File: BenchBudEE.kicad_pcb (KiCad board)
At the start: 4 copper layers, 165.1 x 63.5 mm, 11 parts, among them K1 RELAY, Q1 2N3904, U1 OPTO_TRANSISTOR

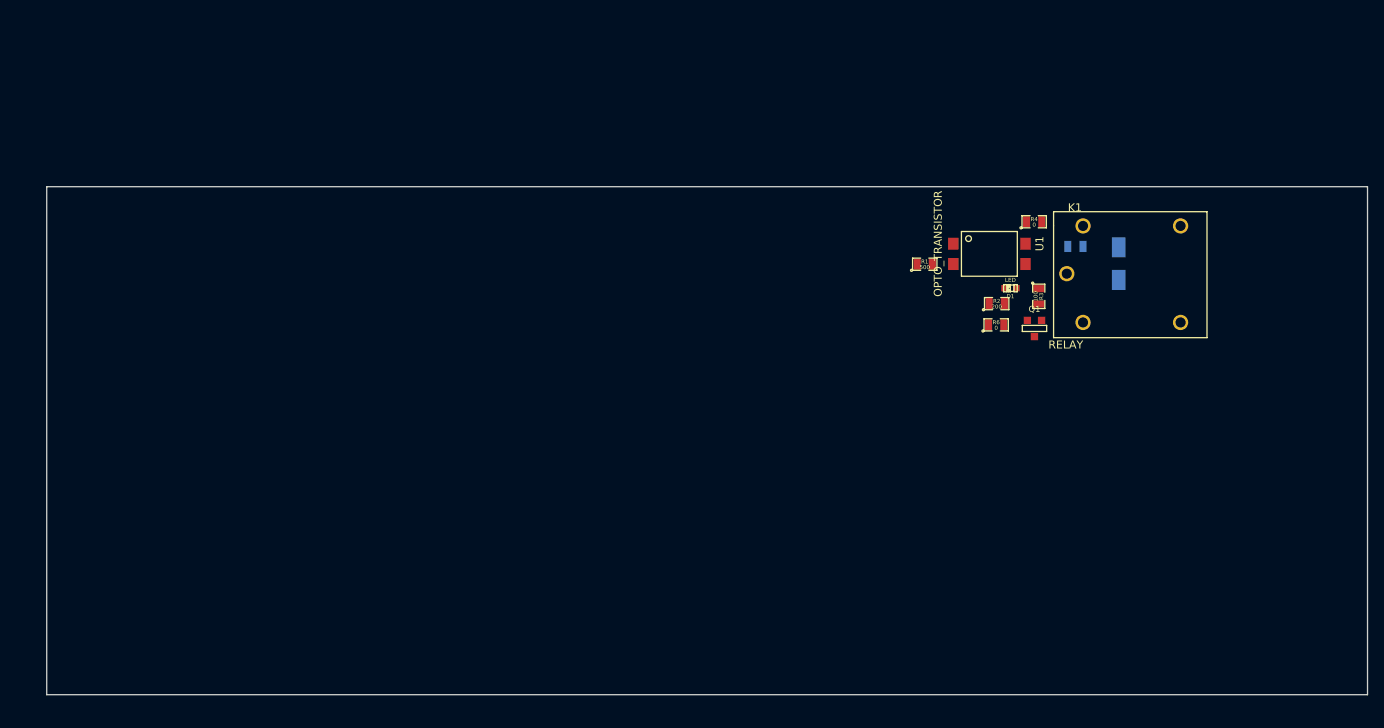
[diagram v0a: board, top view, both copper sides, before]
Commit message: THERMOCOUPLE 02-22-2014
Associated and placed PCB footprints of thermocouple modules in layout
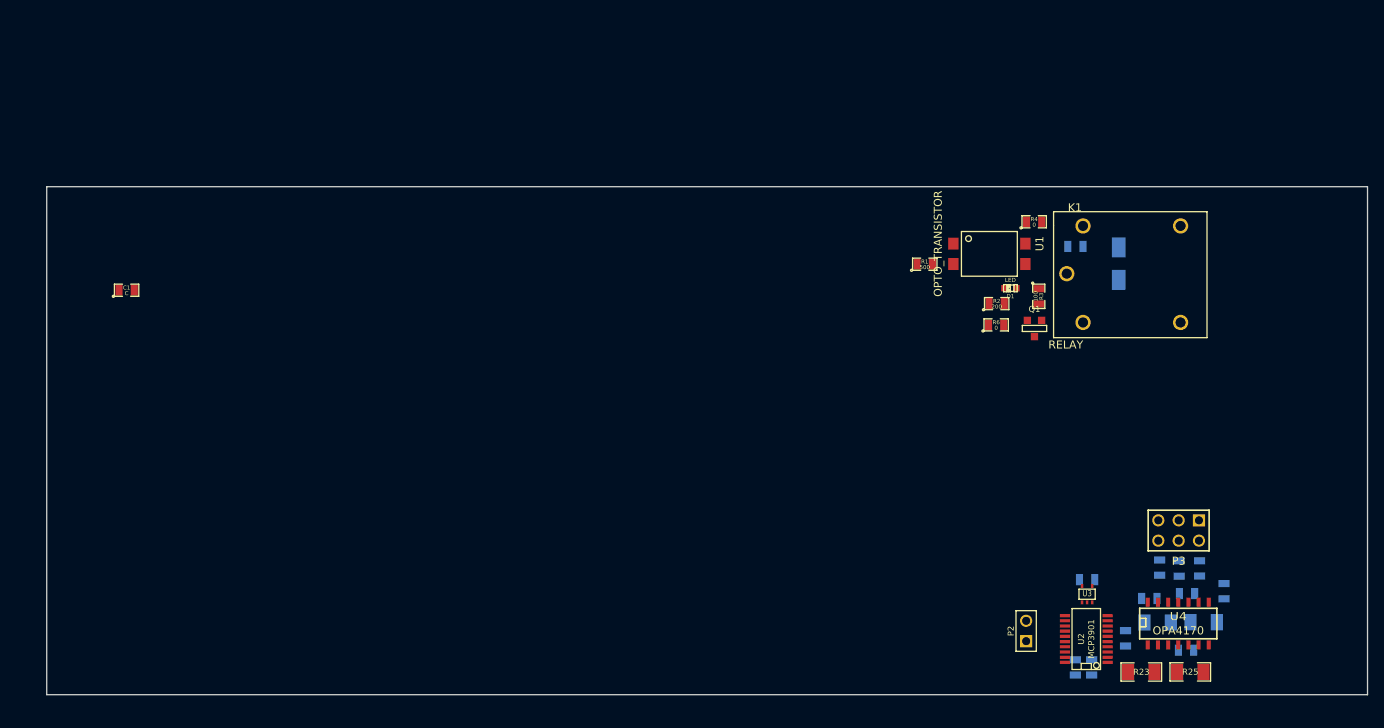
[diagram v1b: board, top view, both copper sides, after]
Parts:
- added C1: C, SM0805, F.Cu at (77.3, 134.1)
- added C10: C, SM0805, B.Cu at (209.7, 179.1)
- added C11: C, SM0805, B.Cu at (209.8, 172.0)
- added C6: C, SM0805, B.Cu at (197.9, 181.2)
- added C7: C, SM0805, B.Cu at (195.9, 181.2)
- added C8: C, SM0805, B.Cu at (202.1, 177.6)
- added C9: C, SM0805, B.Cu at (197.3, 170.2)
- added P2: CONN_2, PIN_ARRAY_2X1, F.Cu at (189.7, 176.7)
- added P3: CONN_3X2, pin_array_3x2, F.Cu at (208.8, 164.1)
- added R23: R, SM1206, F.Cu at (204.1, 181.8)
- added R24: R, SM1206, B.Cu at (211.9, 175.6)
- added R25: R, SM1206, F.Cu at (210.2, 181.8)
- added R26: R, SM1206, B.Cu at (206.2, 175.6)
- added R27: R, SM0805, B.Cu at (214.5, 171.7)
- added R28: R, SM0805, B.Cu at (206.4, 168.7)
- added R29: R, SM0805, B.Cu at (205.1, 172.6)
- added R44: R, SM0805, B.Cu at (208.8, 168.8)
- added R45: R, SM0805, B.Cu at (211.4, 168.8)
- added U2: MCP3901, SSOP20, F.Cu at (197.2, 177.7)
- added U3: LMT84, SOT353, F.Cu at (197.3, 172.1)
- added U4: OPA4170, SO14E, F.Cu at (208.7, 175.6)

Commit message: Terminal Blocks and ATX Connector
Created footprints for 12pin, 3pin terminal blocks and 24pin ATX Header.
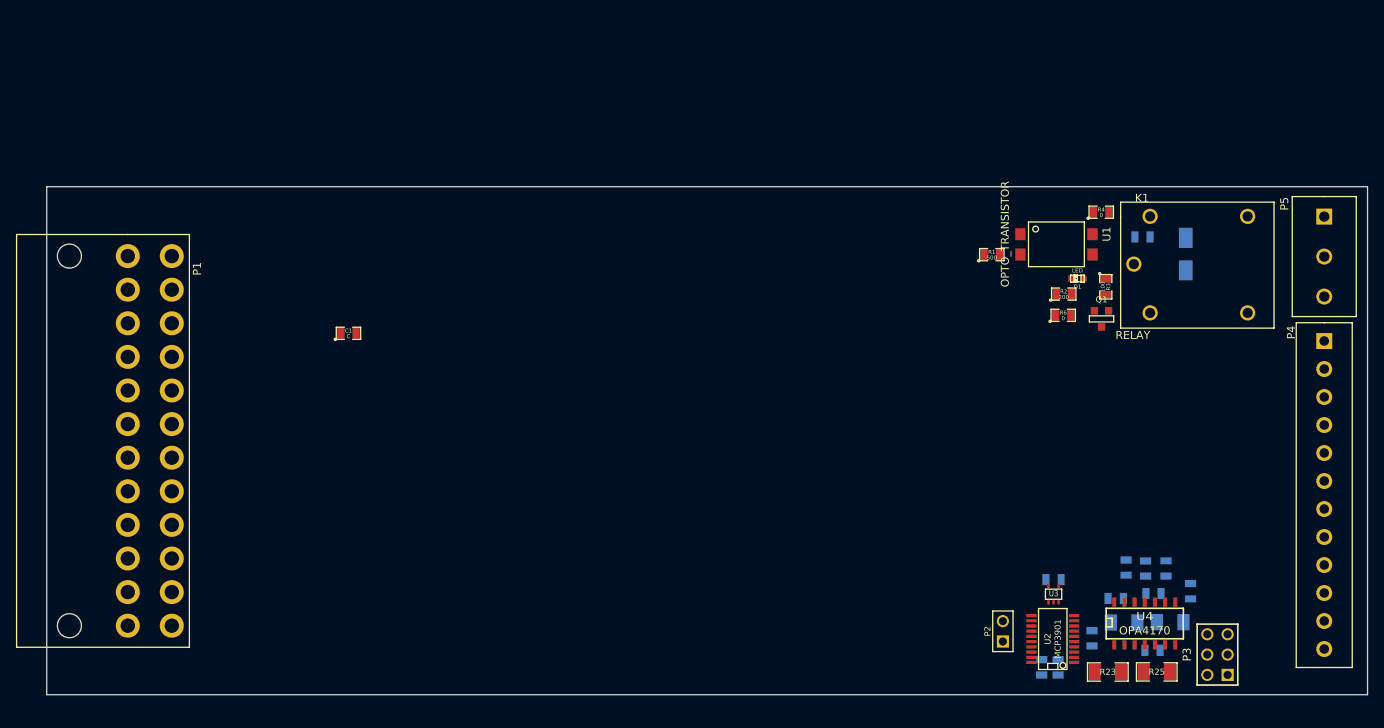
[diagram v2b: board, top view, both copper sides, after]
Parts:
- added P1: 24 Pin MiniFit JR, ATX_Header, F.Cu at (77.4, 129.8)
- added P4: 12 Pin Terminal Block, 12pin_TB, F.Cu at (227.0, 140.4)
- added P5: CONN_3, 3pin_TB, F.Cu at (227.0, 124.9)
- moved C1 28.3 mm to (105.0, 139.4)
- moved P3 16.2 mm to (213.6, 179.6), turned to 90 degrees
- moved D2 8.47 mm to (209.7, 131.6)
- moved Q1 8.47 mm to (199.1, 137.6)
- moved R3 8.47 mm to (199.7, 133.6)
- moved R4 8.47 mm to (199.1, 124.3)
- moved R5 8.47 mm to (204.3, 127.4)
- moved U1 8.47 mm to (189.0, 127.1)
- moved D1 8.47 mm to (196.1, 132.6)
- moved K1 8.47 mm to (203.2, 130.8)
- moved R2 8.47 mm to (194.4, 134.5)
- moved R1 8.47 mm to (185.4, 129.6)
- moved R6 8.47 mm to (194.3, 137.2)
- moved C10 4.19 mm to (205.5, 179.1)
- moved C11 4.19 mm to (205.6, 172.0)
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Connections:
- K1 pad 1: (no net) -> /Relay/RELAY_COM
- K1 pad 3: (no net) -> /Relay/RELAY_NO
- K1 pad 4: (no net) -> /Relay/RELAY_NC
- U4 pad 10: (no net) -> /Terminal_Block/TC_IN_+
- U4 pad 12: (no net) -> /Terminal_Block/TC_IN_-

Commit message: Fan Controller Module
1) Created and associated the footprints of fan controller module
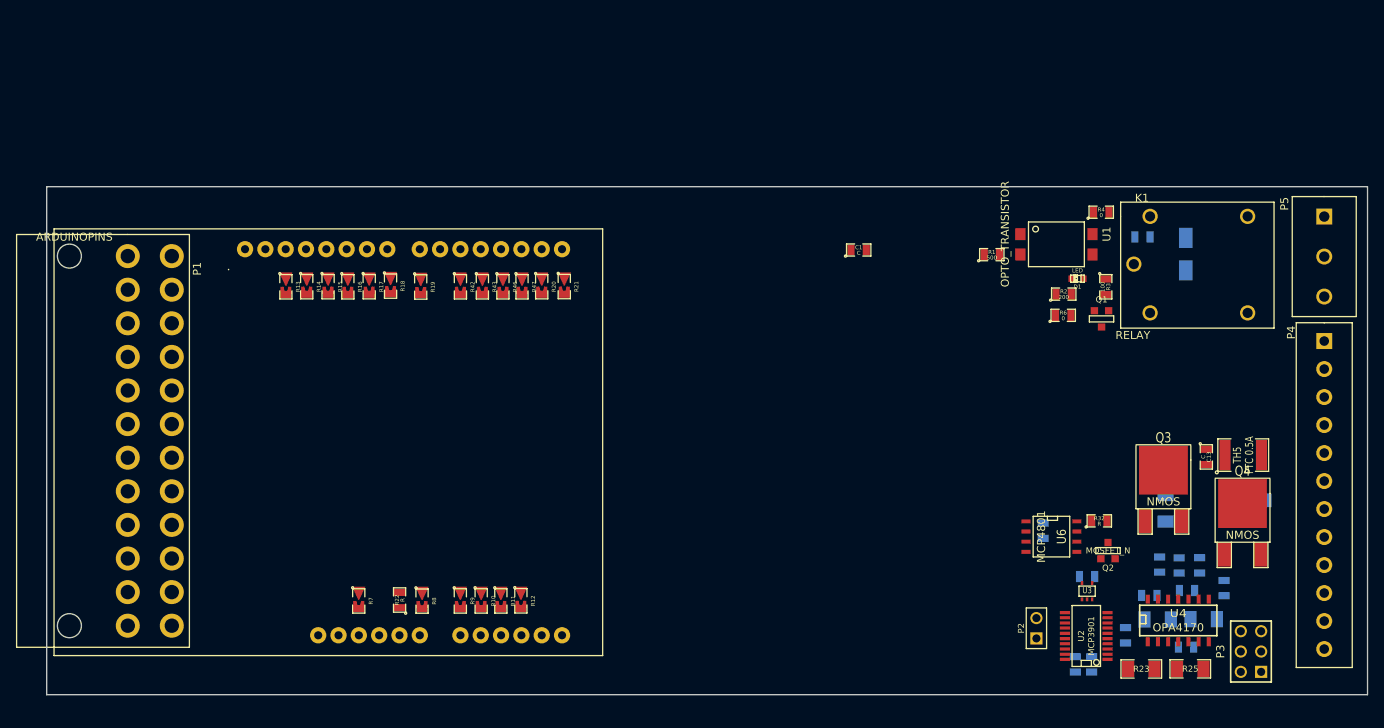
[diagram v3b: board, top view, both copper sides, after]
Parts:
- added ARD1: ARDUINOPINS, ARDUINO, F.Cu at (106.3, 177.2)
- added C12: C, SM0805, B.Cu at (191.8, 164.1)
- added C13: C, SM0805, F.Cu at (212.2, 154.9)
- added D5: Schottky Diode, SMA, B.Cu at (215.1, 160.3)
- added Q2: MOSFET_N, SOT23GDS, F.Cu at (199.9, 166.6)
- added Q3: NMOS, DPAK2, F.Cu at (206.9, 162.9)
- added Q4: NMOS, DPAK2, F.Cu at (216.8, 167.1)
- added R10: R, SM0805-bridge, F.Cu at (121.6, 172.9)
- added R11: R, SM0805-bridge, F.Cu at (124.1, 172.9)
- added R12: R, SM0805-bridge, F.Cu at (126.6, 172.9)
- added R13: R, SM0805-bridge, F.Cu at (97.2, 133.6)
- added R14: R, SM0805-bridge, F.Cu at (99.8, 133.6)
- added R15: R, SM0805-bridge, F.Cu at (102.5, 133.6)
- added R16: R, SM0805-bridge, F.Cu at (104.9, 133.6)
- added R17: R, SM0805-bridge, F.Cu at (107.6, 133.6)
- added R18: R, SM0805-bridge, F.Cu at (110.3, 133.5)
- added R19: R, SM0805-bridge, F.Cu at (114.0, 133.7)
- added R20: R, SM0805-bridge, F.Cu at (129.2, 133.6)
- added R21: R, SM0805-bridge, F.Cu at (132.0, 133.6)
- added R22: R, SM0805, F.Cu at (111.4, 172.8)
- added R32: R, SM0805, F.Cu at (198.9, 162.9)
- added R33: R, SM1206, B.Cu at (207.1, 161.3)
- added R42: R, SM0805-bridge, F.Cu at (119.0, 133.6)
- added R43: R, SM0805-bridge, F.Cu at (121.7, 133.6)
- added R46: R, SM0805-bridge, F.Cu at (124.3, 133.6)
- added R47: R, SM0805-bridge, F.Cu at (126.7, 133.6)
- added R7: R, SM0805-bridge, F.Cu at (106.3, 172.9)
- added R8: R, SM0805-bridge, F.Cu at (114.2, 172.9)
- added R9: R, SM0805-bridge, F.Cu at (119.0, 172.9)
- added TH5: PTC 0.5A, SM1812, F.Cu at (216.8, 154.7)
- added U6: MCP4801, SO8N, F.Cu at (192.9, 164.9)
- moved C1 64.6 mm to (168.8, 129.0)
- moved C10 4.21 mm to (209.7, 178.7)
- moved C11 4.21 mm to (209.8, 171.6)
- moved C6 4.21 mm to (197.9, 180.8)
- moved C7 4.21 mm to (195.9, 180.8)
- moved C9 4.21 mm to (197.3, 169.8)
- moved P3 4.21 mm to (217.8, 179.2)
- moved R23 4.21 mm to (204.1, 181.4)
- moved R25 4.21 mm to (210.2, 181.4)
- moved R26 4.21 mm to (206.2, 175.2)
- moved R27 4.21 mm to (214.5, 171.3)
- moved R28 4.21 mm to (206.4, 168.4)
- moved R29 4.21 mm to (205.1, 172.2)
- moved R44 4.21 mm to (208.8, 168.5)
- moved R45 4.21 mm to (211.4, 168.5)
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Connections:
- U2 pad 17: /Arduino/ADC_CS_N -> /Arduino/~ADC_CS

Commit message: Power Filter Module
Created and associated footprints for PCB layout
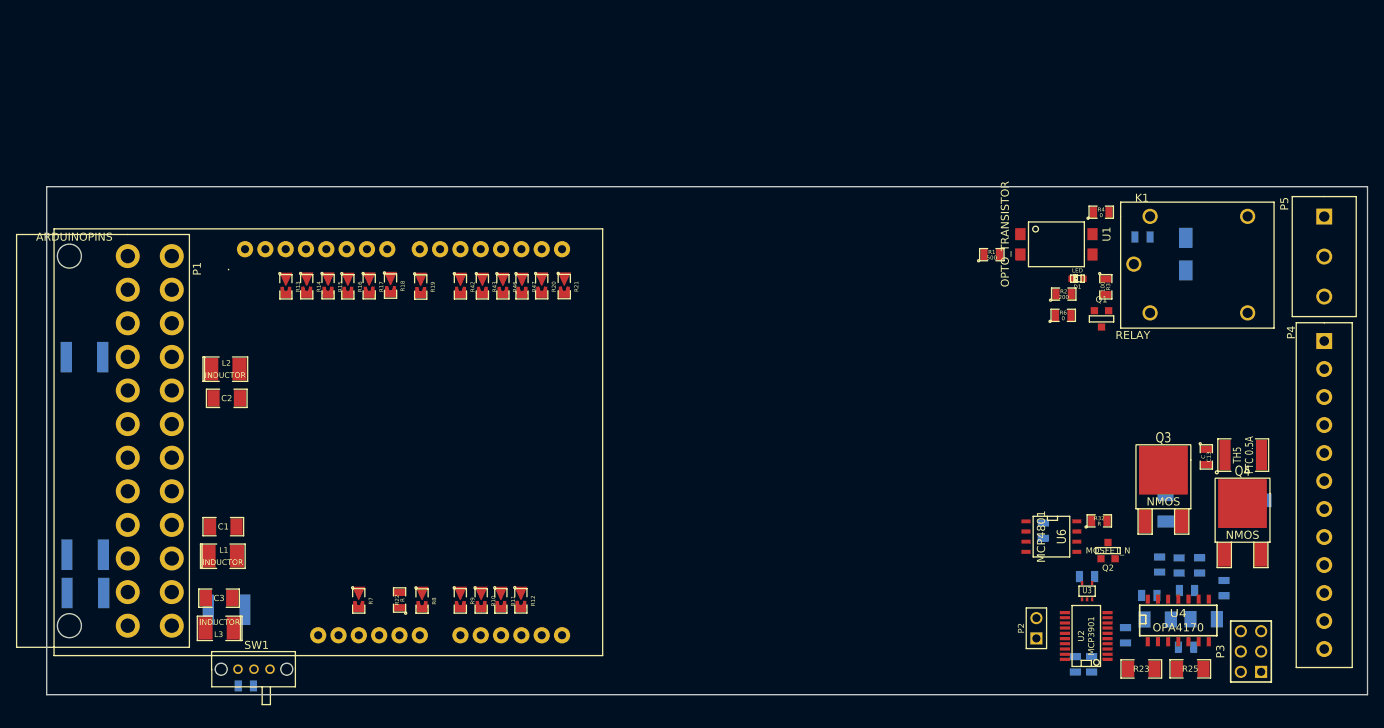
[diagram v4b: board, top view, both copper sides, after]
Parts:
- added C2: C, SM1206, F.Cu at (89.8, 147.6)
- added C3: C, SM1206, F.Cu at (88.8, 172.6)
- added L1: INDUCTOR, SM1210L, F.Cu at (89.3, 167.3)
- added L2: INDUCTOR, SM1210L, F.Cu at (89.6, 143.9)
- added L3: INDUCTOR, SM1210L, F.Cu at (88.9, 176.3)
- added R30: R, SM0805, B.Cu at (92.2, 183.5)
- added SW1: SWITCH, SPDT_SW, F.Cu at (93.2, 181.4)
- added TH1: THERMISTOR, SM1812, B.Cu at (72.1, 171.9)
- added TH2: THERMISTOR, SM1812, B.Cu at (72.1, 167.1)
- added TH3: THERMISTOR, SM1812, B.Cu at (72.0, 142.4)
- added TH4: THERMISTOR, SM1812, B.Cu at (89.8, 174.0)
- C1: footprint SM0805 -> SM1206
- moved C1 86.6 mm to (89.4, 163.6), turned to 180 degrees

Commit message: Completed placement and association of all footprints
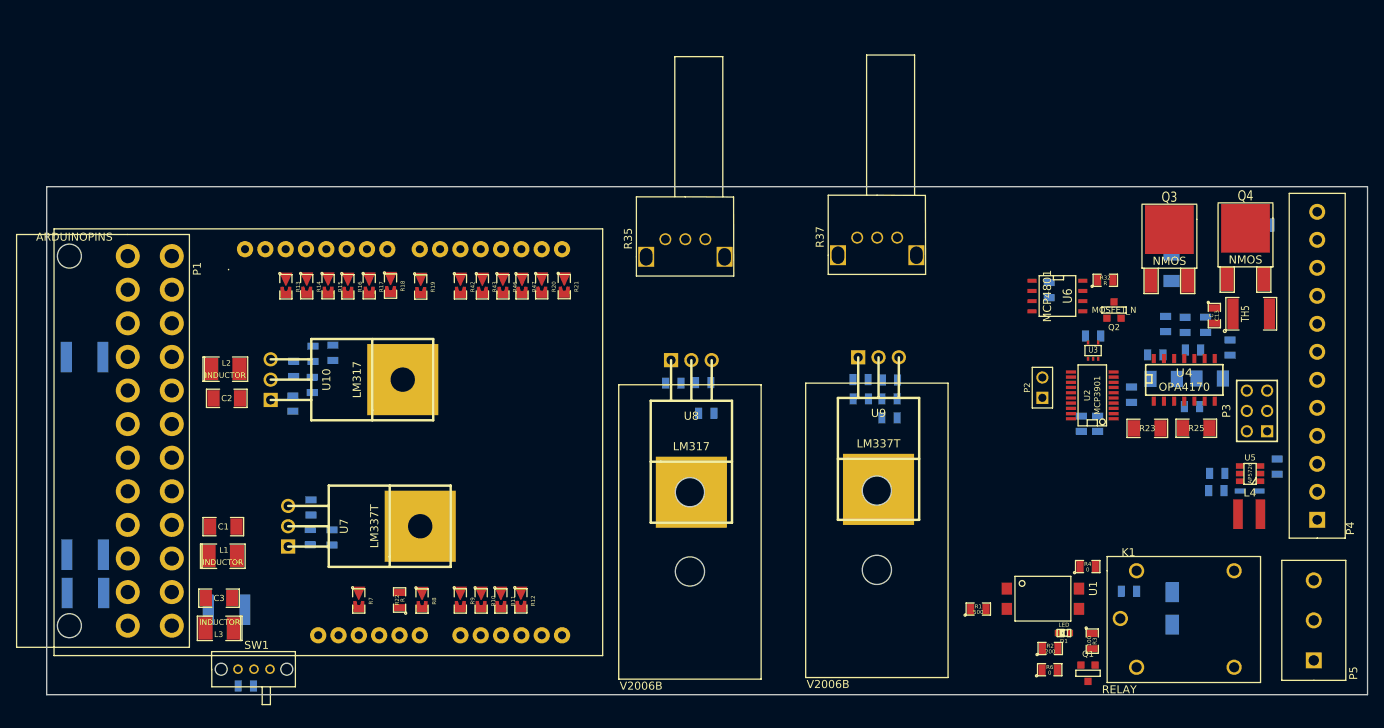
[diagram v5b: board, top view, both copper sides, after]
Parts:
- added C14: C, SM0805, B.Cu at (169.0, 145.2)
- added C15: C, SM0805, B.Cu at (98.0, 148.2)
- added C16: C, SM0805, B.Cu at (100.3, 161.2)
- added C17: C, SM0805, B.Cu at (100.5, 145.9)
- added C18: C, SM0805, B.Cu at (145.6, 145.7)
- added C19: C, SM0805, B.Cu at (172.6, 150.0)
- added C4: 1u, SM0805, B.Cu at (213.5, 159.1)
- added C5: 1u, SM0805, B.Cu at (213.6, 157.0)
- added D4: B0540WS-7, SOD323, B.Cu at (218.8, 159.2)
- added L4: 22uH, NR4012, F.Cu at (216.2, 162.1)
- added R31: 15, SM0805, B.Cu at (221.1, 156.1)
- added R34: R, SM0805, B.Cu at (149.3, 145.6)
- added R35: RVAR, POT_EVUE3K, F.Cu at (147.1, 127.7)
- added R36: R, SM0805, B.Cu at (172.7, 145.3)
- added R37: RVAR, POT_EVUE3K, F.Cu at (171.1, 127.5)
- added R38: R, SM0805, B.Cu at (149.7, 149.4)
- added R39: R, SM0805, B.Cu at (103.0, 141.9)
- added R40: R, SM0805, B.Cu at (172.6, 147.6)
- added R41: R, SM0805, B.Cu at (169.0, 147.6)
- added R48: R, SM0805, B.Cu at (102.9, 165.0)
- added R49: R, SM0805, B.Cu at (100.2, 164.9)
- added R50: R, SM0805, B.Cu at (98.1, 143.9)
- added R51: R, SM0805, B.Cu at (100.6, 142.0)
- added U10: LM317, TO220, F.Cu at (95.3, 145.2)
- added U5: AP5726, SOT23_6, F.Cu at (217.7, 157.0)
- added U7: LM337T, TO220, F.Cu at (97.5, 163.6)
- added U8: LM317, TO220, F.Cu at (147.9, 142.8)
- added U9: LM337T, TO220, F.Cu at (171.3, 142.4)
- added V2006B: VAL**, V2006B, F.Cu at (162.2, 182.5)
- added V2006B: VAL**, V2006B, F.Cu at (138.8, 182.7)
- moved P5 55.5 mm to (225.7, 180.3), turned to 90 degrees
- moved Q1 44.3 mm to (197.4, 181.9)
- moved R1 44.3 mm to (183.7, 173.9)
- moved R5 44.3 mm to (202.6, 171.7)
- moved R4 44.3 mm to (197.4, 168.6)
- moved U1 44.3 mm to (187.3, 171.3)
- moved D1 44.3 mm to (194.4, 176.9)
- moved D2 44.3 mm to (208.0, 175.9)
- moved K1 44.3 mm to (201.5, 175.1)
- moved R2 44.3 mm to (192.7, 178.8)
- moved R3 44.3 mm to (198.0, 177.9)
- moved R6 44.3 mm to (192.7, 181.5)
- moved D5 34.4 mm to (215.4, 125.9)
- moved Q4 34.4 mm to (217.1, 132.7)
- moved C10 30.1 mm to (210.4, 148.6)
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
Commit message: Layout v1.0
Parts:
- removed V2006B (x2): VAL**, V2006B
- added 3mm_drill: VAL**, 3mm_drill, F.Cu at (80.1, 124.1)
- added 3mm_drill: VAL**, 3mm_drill, F.Cu at (80.3, 181.6)
- added 3mm_drill: VAL**, 3mm_drill, F.Cu at (218.1, 126.2)
- added JP1: JUMPER, PIN_ARRAY_2X1, F.Cu at (212.5, 162.3)
- U10, U8: value LM317 -> LM317K; footprint TO220 -> TO220_VERT
- U7, U9: footprint TO220 -> TO220_VERT
- moved R49 85.2 mm to (179.9, 134.7), turned to 0 degrees
- moved R48 83.8 mm to (180.0, 132.0), turned to 180 degrees
- moved U10 83.2 mm to (178.4, 148.9), turned to 90 degrees
- moved C16 80.4 mm to (176.2, 134.7), turned to 0 degrees
- moved C15 71.0 mm to (167.9, 135.8), turned to 0 degrees
- moved U7 68.6 mm to (164.6, 149.4), turned to 90 degrees
- moved C17 66.3 mm to (165.6, 133.4), turned to 0 degrees
- moved R50 65.9 mm to (163.6, 135.7), turned to 180 degrees
- moved R51 61.8 mm to (161.7, 133.3), turned to 180 degrees
- moved R39 59.6 mm to (161.6, 130.8), turned to 180 degrees
- moved C6 53.0 mm to (148.0, 166.5)
- moved C7 53.0 mm to (146.0, 166.5)
- moved U2 53.0 mm to (147.3, 162.9)
- moved P2 53.0 mm to (141.1, 162.0)
- moved C8 53.0 mm to (152.2, 162.8)
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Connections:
- C13 pad 2: AGND -> GND
- K1 pad 3: /Relay/RELAY_NO -> /Relay/RELAY_NC
- K1 pad 4: /Relay/RELAY_NC -> /Relay/RELAY_NO
- Q3 pad 3: AGND -> GND
- R33 pad 2: AGND -> GND
- R34 pad 2: N-00000118 (its old number) -> N-00000120
- R35 pad 1: N-00000118 (its old number) -> N-00000120
- R50 pad 2: N-00000122 -> N-00000121
- R51 pad 1: N-00000122 -> N-00000121
- TH1 pad 2: (no net) -> +3.3V
- U10 pad 1: +12V -> N-00000120
- U10 pad 2: N-00000122 -> +12V
- U10 pad 3: FE_V+ -> /Power_Adjustment_Monitor/V+_ADJ
- U4 pad 11: -12V -> FE_V-
- U4 pad 4: +12V -> FE_V+
- U8 pad 1: +12V -> N-00000121
- U8 pad 2: N-00000118 (its old number) -> +12V
- U8 pad 3: /Power_Adjustment_Monitor/V+_ADJ -> FE_V+
- U9 pad 2: /Power_Adjustment_Monitor/V-_ADJ -> -12V
- U9 pad 3: -12V -> /Power_Adjustment_Monitor/V-_ADJ

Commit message: Layout v2.0
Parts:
- D5: moved to F.Cu
- moved R30 62.5 mm to (103.5, 122.5), turned to 180 degrees
- moved SW1 58.7 mm to (102.5, 124.6), turned to 180 degrees
- moved U7 50.8 mm to (210.3, 127.4)
- moved JP1 46.0 mm to (167.0, 169.8), turned to 270 degrees
- moved C17 41.9 mm to (124.4, 125.5)
- moved R51 41.9 mm to (120.6, 125.4)
- moved C15 41.9 mm to (126.8, 128.0)
- moved R39 41.9 mm to (120.4, 122.9)
- moved R50 41.9 mm to (122.4, 127.9)
- moved U10 36.7 mm to (150.4, 125.2)
- moved C18 36.4 mm to (157.5, 123.8)
- moved R34 36.4 mm to (161.3, 123.8)
- moved R38 36.4 mm to (161.7, 127.6)
- moved C19 30.8 mm to (186.6, 137.7)
- moved R36 30.8 mm to (186.7, 133.0)
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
